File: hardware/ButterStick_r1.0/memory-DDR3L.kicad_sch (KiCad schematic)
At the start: 3 parts

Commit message: hw.r1d0: Review complete, gerbers generated
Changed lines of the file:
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@@
 (kicad_sch (version 20200618) (host eeschema "5.99.0-unknown-73168a9~101~ubuntu18.04.1")
-  (page 13 18)
+  (page 1 18)
   (paper "A4")
   (title_block
     (title "ButterStick")
-    (date "2020-07-16")
+    (date "2020-07-17")
     (rev "r1.0")
     (company "GsD")
@@
     (stroke (width 0) (type solid) (color 0 0 0 0))
   )
-  (bus (pts (xy 80.01 104.14) (xy 80.01 106.68))
+  (bus (pts (xy 80.01 104.14) (xy 80.01 109.22))
     (stroke (width 0) (type solid) (color 0 0 0 0))
   )
-  (bus (pts (xy 80.01 106.68) (xy 80.01 111.76))
+  (bus (pts (xy 80.01 109.22) (xy 80.01 111.76))
     (stroke (width 0) (type solid) (color 0 0 0 0))
   )

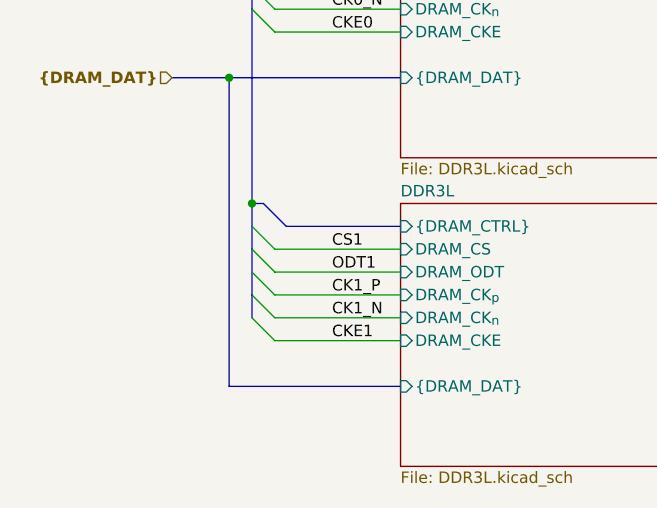
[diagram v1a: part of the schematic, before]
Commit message: hw.r1d0: Update BOM fieids in schematic.
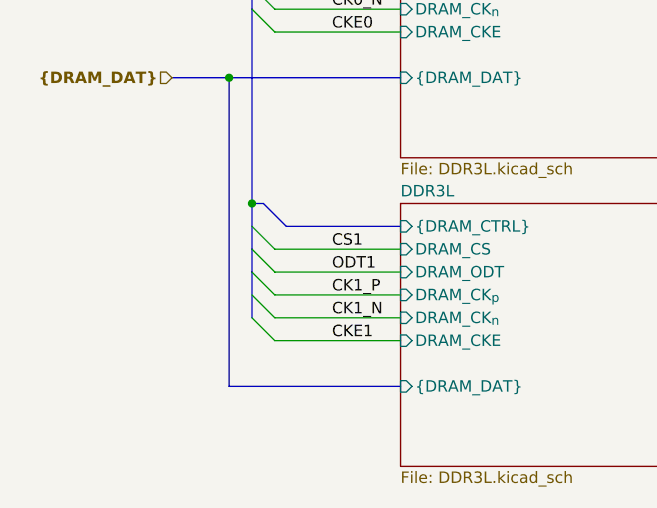
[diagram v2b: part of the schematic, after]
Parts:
- C119: Mfg (none) -> Yageo; PN (none) -> CC0402MRX5R6BB475
- R69, R70: Mfg (none) -> Yageo; PN (none) -> RC0402FR-071KL
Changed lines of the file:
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@@
     (stroke (width 0) (type solid) (color 0 0 0 0))
   )
-  (bus (pts (xy 80.01 104.14) (xy 80.01 109.22))
+  (bus (pts (xy 80.01 104.14) (xy 80.01 106.68))
     (stroke (width 0) (type solid) (color 0 0 0 0))
   )
-  (bus (pts (xy 80.01 109.22) (xy 80.01 111.76))
+  (bus (pts (xy 80.01 106.68) (xy 80.01 111.76))
     (stroke (width 0) (type solid) (color 0 0 0 0))
   )
@@
       (effects (font (size 1.27 1.27)) hide)
     )
+    (property "Mfg" "Yageo" (id 4) (at 177.8 91.44 0)
+      (effects (font (size 1.27 1.27)) hide)
+    )
+    (property "PN" "RC0402FR-071KL" (id 4) (at 177.8 91.44 0)
+      (effects (font (size 1.27 1.27)) hide)
+    )
   )
   (symbol (lib_id "Device:R") (at 177.8 101.6 0) (mirror y) (unit 1)
@@
     )
     (property "Datasheet" "~" (id 3) (at 177.8 101.6 0)
+      (effects (font (size 1.27 1.27)) hide)
+    )
+    (property "Mfg" "Yageo" (id 4) (at 177.8 101.6 0)
+      (effects (font (size 1.27 1.27)) hide)
+    )
+    (property "PN" "RC0402FR-071KL" (id 4) (at 177.8 101.6 0)
       (effects (font (size 1.27 1.27)) hide)
     )
@@
       (effects (font (size 1.27 1.27)) hide)
     )
+    (property "Mfg" "Yageo" (id 4) (at 171.45 101.6 0)
+      (effects (font (size 1.27 1.27)) hide)
+    )
+    (property "PN" "CC0402MRX5R6BB475" (id 4) (at 171.45 101.6 0)
+      (effects (font (size 1.27 1.27)) hide)
+    )

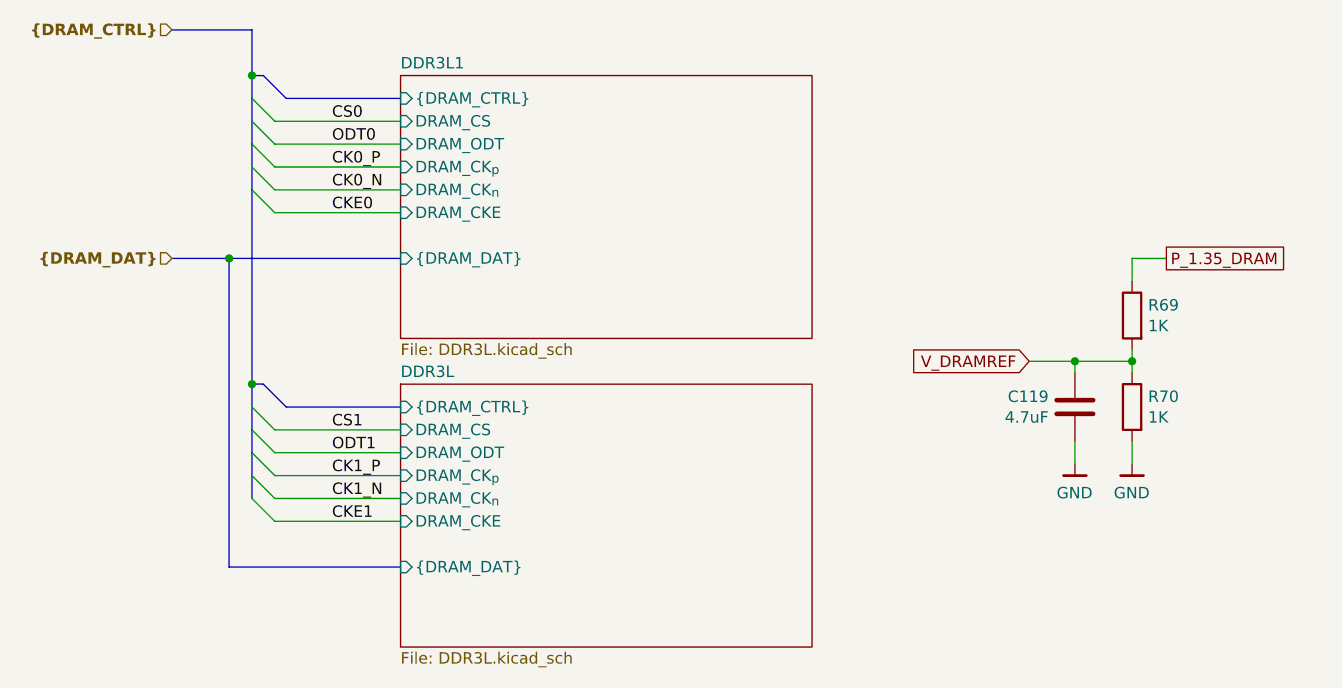
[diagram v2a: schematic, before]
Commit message: hw.r1d0: Fix RGMII straps
This commit correctly sets the stop resistos on the RGMII lines to 1K5
instead of DNP.
Also regenerate and add a schematic in PDF format.

Fixes #6
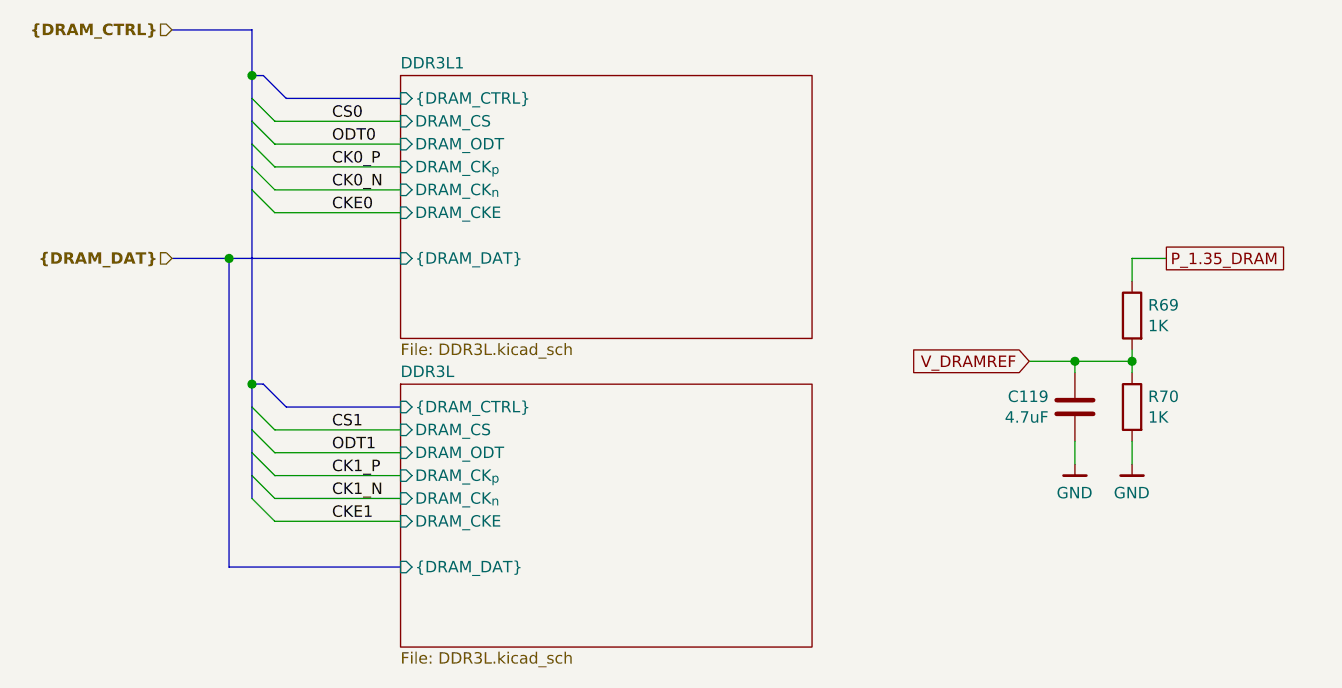
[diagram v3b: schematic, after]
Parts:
- C119: PN CC0402MRX5R6BB475 -> CC0402KRX5R6BB475
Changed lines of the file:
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@@
-(kicad_sch (version 20200618) (host eeschema "5.99.0-unknown-73168a9~101~ubuntu18.04.1")
+(kicad_sch (version 20201015) (generator eeschema)
   (page 1 18)
   (paper "A4")
   (title_block
     (title "ButterStick")
-    (date "2020-07-17")
+    (date "2020-11-01")
     (rev "r1.0")
     (company "GsD")
     (comment 1 "Functional prototyping board for the Lattice ECP5.")
-  )
-  (junction (at 171.45 96.52) (diameter 0) (color 0 0 0 0))
-  (junction (at 177.8 96.52) (diameter 0) (color 0 0 0 0))
-  (junction (at 77.47 85.09) (diameter 0) (color 0 0 0 0))
-  (junction (at 80.01 64.77) (diameter 0) (color 0 0 0 0))
-  (junction (at 80.01 99.06) (diameter 0) (color 0 0 0 0))
+    (comment 2 "SYZYGY compatible")
+  )
+  (junction (at 171.45 96.52) (diameter 1.016) (color 0 0 0 0))
+  (junction (at 177.8 96.52) (diameter 1.016) (color 0 0 0 0))
+  (junction (at 77.47 85.09) (diameter 1.016) (color 0 0 0 0))
+  (junction (at 80.01 64.77) (diameter 1.016) (color 0 0 0 0))
+  (junction (at 80.01 99.06) (diameter 1.016) (color 0 0 0 0))
   (bus_entry (at 80.01 67.31) (size 2.54 2.54)
     (stroke (width 0.1524) (type solid) (color 0 0 0 0))
@@
     (stroke (width 0) (type solid) (color 0 0 0 0))
   )
-  (bus (pts (xy 80.01 67.31) (xy 80.01 72.39))
-    (stroke (width 0) (type solid) (color 0 0 0 0))
-  )
-  (bus (pts (xy 80.01 72.39) (xy 80.01 77.47))
+  (bus (pts (xy 80.01 67.31) (xy 80.01 69.85))
+    (stroke (width 0) (type solid) (color 0 0 0 0))
+  )
+  (bus (pts (xy 80.01 69.85) (xy 80.01 72.39))
+    (stroke (width 0) (type solid) (color 0 0 0 0))
+  )
+  (bus (pts (xy 80.01 72.39) (xy 80.01 74.93))
+    (stroke (width 0) (type solid) (color 0 0 0 0))
+  )
+  (bus (pts (xy 80.01 74.93) (xy 80.01 77.47))
     (stroke (width 0) (type solid) (color 0 0 0 0))
   )
@@
     (stroke (width 0) (type solid) (color 0 0 0 0))
   )
-  (bus (pts (xy 80.01 99.06) (xy 80.01 104.14))
+  (bus (pts (xy 80.01 99.06) (xy 80.01 101.6))
     (stroke (width 0) (type solid) (color 0 0 0 0))
   )
@@
     (stroke (width 0) (type solid) (color 0 0 0 0))
   )
+  (bus (pts (xy 80.01 101.6) (xy 80.01 104.14))
+    (stroke (width 0) (type solid) (color 0 0 0 0))
+  )
   (bus (pts (xy 80.01 104.14) (xy 80.01 106.68))
     (stroke (width 0) (type solid) (color 0 0 0 0))
   )
-  (bus (pts (xy 80.01 106.68) (xy 80.01 111.76))
+  (bus (pts (xy 80.01 106.68) (xy 80.01 109.22))
+    (stroke (width 0) (type solid) (color 0 0 0 0))
+  )
+  (bus (pts (xy 80.01 109.22) (xy 80.01 111.76))
     (stroke (width 0) (type solid) (color 0 0 0 0))
   )
@@
       (effects (font (size 1.27 1.27)) hide)
     )
-    (property "PN" "CC0402MRX5R6BB475" (id 4) (at 171.45 101.6 0)
-      (effects (font (size 1.27 1.27)) hide)
-    )
+    (property "PN" "CC0402KRX5R6BB475" (id 4) (at 171.45 101.6 0)
+      (effects (font (size 1.27 1.27)) hide)
+    )
